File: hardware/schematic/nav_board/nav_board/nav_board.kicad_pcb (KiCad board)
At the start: 2 copper layers, 144 x 52 mm, 5 parts, among them J1 Screw_Terminal_01x04, J2 Screw_Terminal_01x03

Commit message: First order of PCBs
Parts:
- moved J1 5.00 mm to (105.0, 62.5)
- moved J2 4.97 mm to (83.0, 62.5)
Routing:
- net +5V: track 136.7 -> 126.9 mm
- net Net-(A1-DAC2/A0): track 81.6 -> 74.0 mm
- net Net-(A1-DAC1/A1): track 87.1 -> 79.6 mm
- net GND: track 140.1 -> 132.9 mm
- net Net-(A1-I34/A2): track 52.7 -> 49.8 mm
- net Net-(A1-SCL/IO22): track 106.3 -> 104.5 mm
- net Net-(A1-SDA/IO23): track 95.6 -> 94.4 mm
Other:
- board size 144 x 52 mm -> 137 x 42.5 mm
- board text added: "+5V"
- board text added: "Flow"
- board text added: "GND"
- board text added: "RX"
- board text added: "TX"

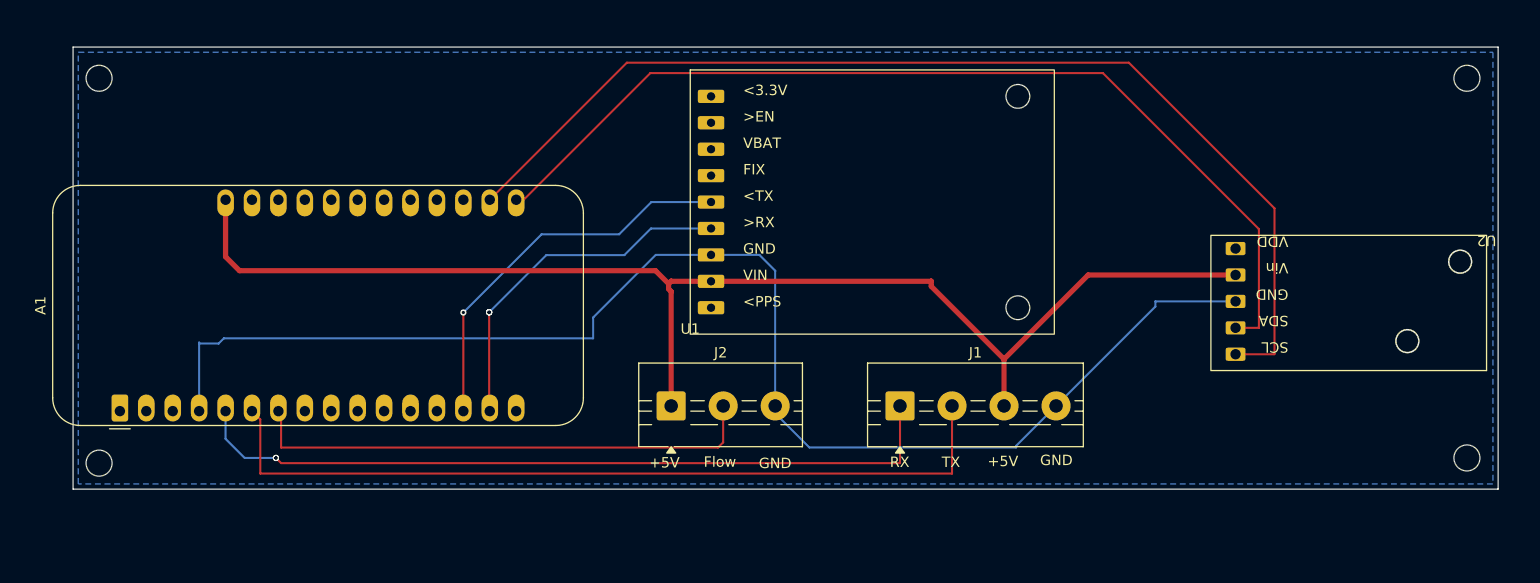
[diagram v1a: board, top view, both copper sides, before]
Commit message: Updating nav board, and also K-factor for speed cal
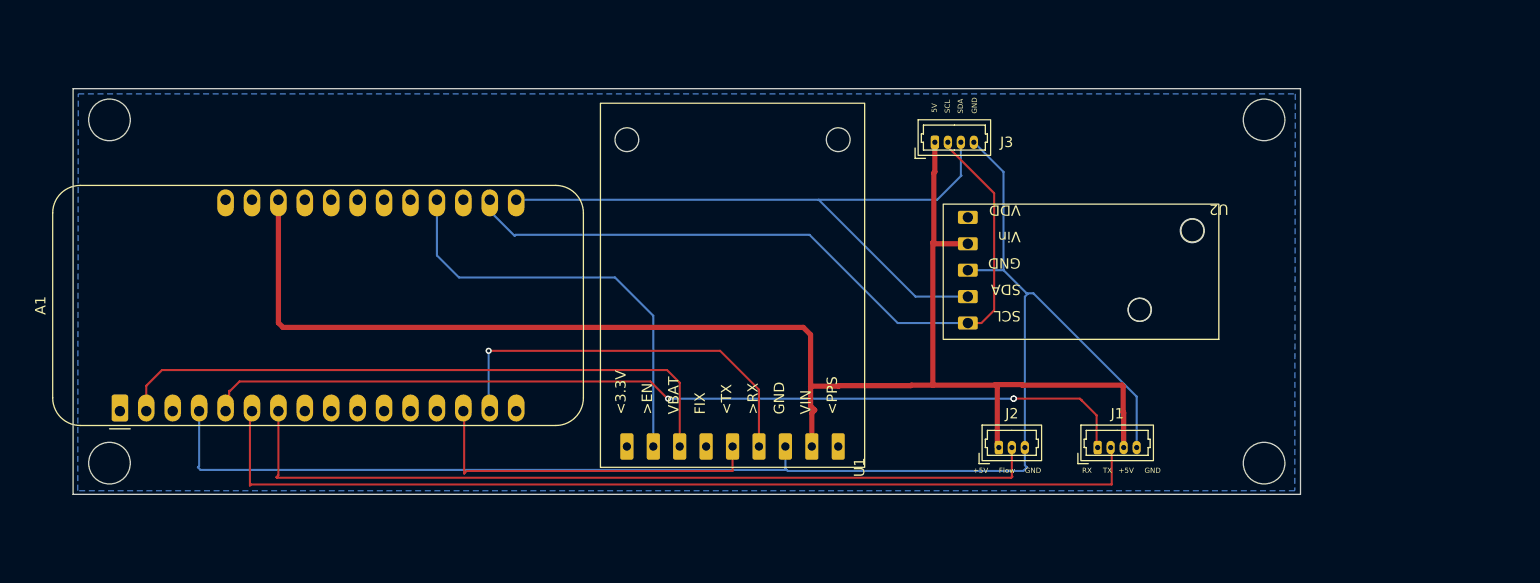
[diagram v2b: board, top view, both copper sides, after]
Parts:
- added J3: Depth Sensor, Connector_Molex:Molex_PicoBlade_53047-0410_1x04_P1.25mm_Vertical, F.Cu at (108.3, 37.1)
- J1: value Screw_Terminal_01x04 -> RS232 to Display; footprint TerminalBlock:TerminalBlock_MaiXu_MX126-5.0-04P_1x04_P5.00mm -> Connector_Molex:Molex_PicoBlade_53047-0410_1x04_P1.25mm_Vertical
- J2: value Screw_Terminal_01x03 -> Flow Meter; footprint TerminalBlock:TerminalBlock_MaiXu_MX126-5.0-03P_1x03_P5.00mm -> Connector_Molex:Molex_PicoBlade_53047-0310_1x03_P1.25mm_Vertical
- moved J2 31.8 mm to (114.5, 66.5)
- moved U2 25.9 mm to (135.7, 43.1)
- moved U1 21.1 mm to (101.6, 68.4), turned to 90 degrees
- moved J1 19.4 mm to (124.0, 66.5)
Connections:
- A1 pad 2: unconnected-(A1-3V3-Pad2) -> Net-(A1-3V3)
- A1 pad 20: unconnected-(A1-A7/IO32-Pad20) -> Net-(A1-A7/IO32)
- A1 pad 26: unconnected-(A1-USB-Pad26) -> +5V
- A1 pad 28: +5V -> unconnected-(A1-VBAT-Pad28)
- U1 pad 7: unconnected-(U1-VBAT-Pad7) -> Net-(A1-3V3)
- U1 pad 8: unconnected-(U1-EN-Pad8) -> Net-(A1-A7/IO32)
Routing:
- net Net-(A1-3V3): track 0.00 -> 61.0 mm
- net Net-(A1-A7/IO32): track 0.00 -> 41.1 mm
- net Net-(A1-SCL/IO22): track 104.5 -> 72.6 mm
- net Net-(A1-I34/A2): track 49.8 -> 80.1 mm
- net Net-(A1-SDA/IO23): track 94.4 -> 65.2 mm
- net +5V: track 126.9 -> 143.7 mm
- net Net-(A1-DAC2/A0): track 74.0 -> 90.5 mm
- net Net-(A1-DAC1/A1): track 79.6 -> 93.8 mm
- net GND: track 132.9 -> 144.3 mm
- net Net-(A1-TX/IO17): track 34.2 -> 38.8 mm, vias 3 -> 1
- net Net-(A1-RX/IO16): track 37.7 -> 34.3 mm, vias 1 -> 0
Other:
- board size 137 x 42.5 mm -> 118 x 39 mm
- board text added: "5V"
- board text added: "SCL"
- board text added: "SDA"
